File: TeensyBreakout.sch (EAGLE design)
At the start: 74 parts, among them IC1 MCP73871

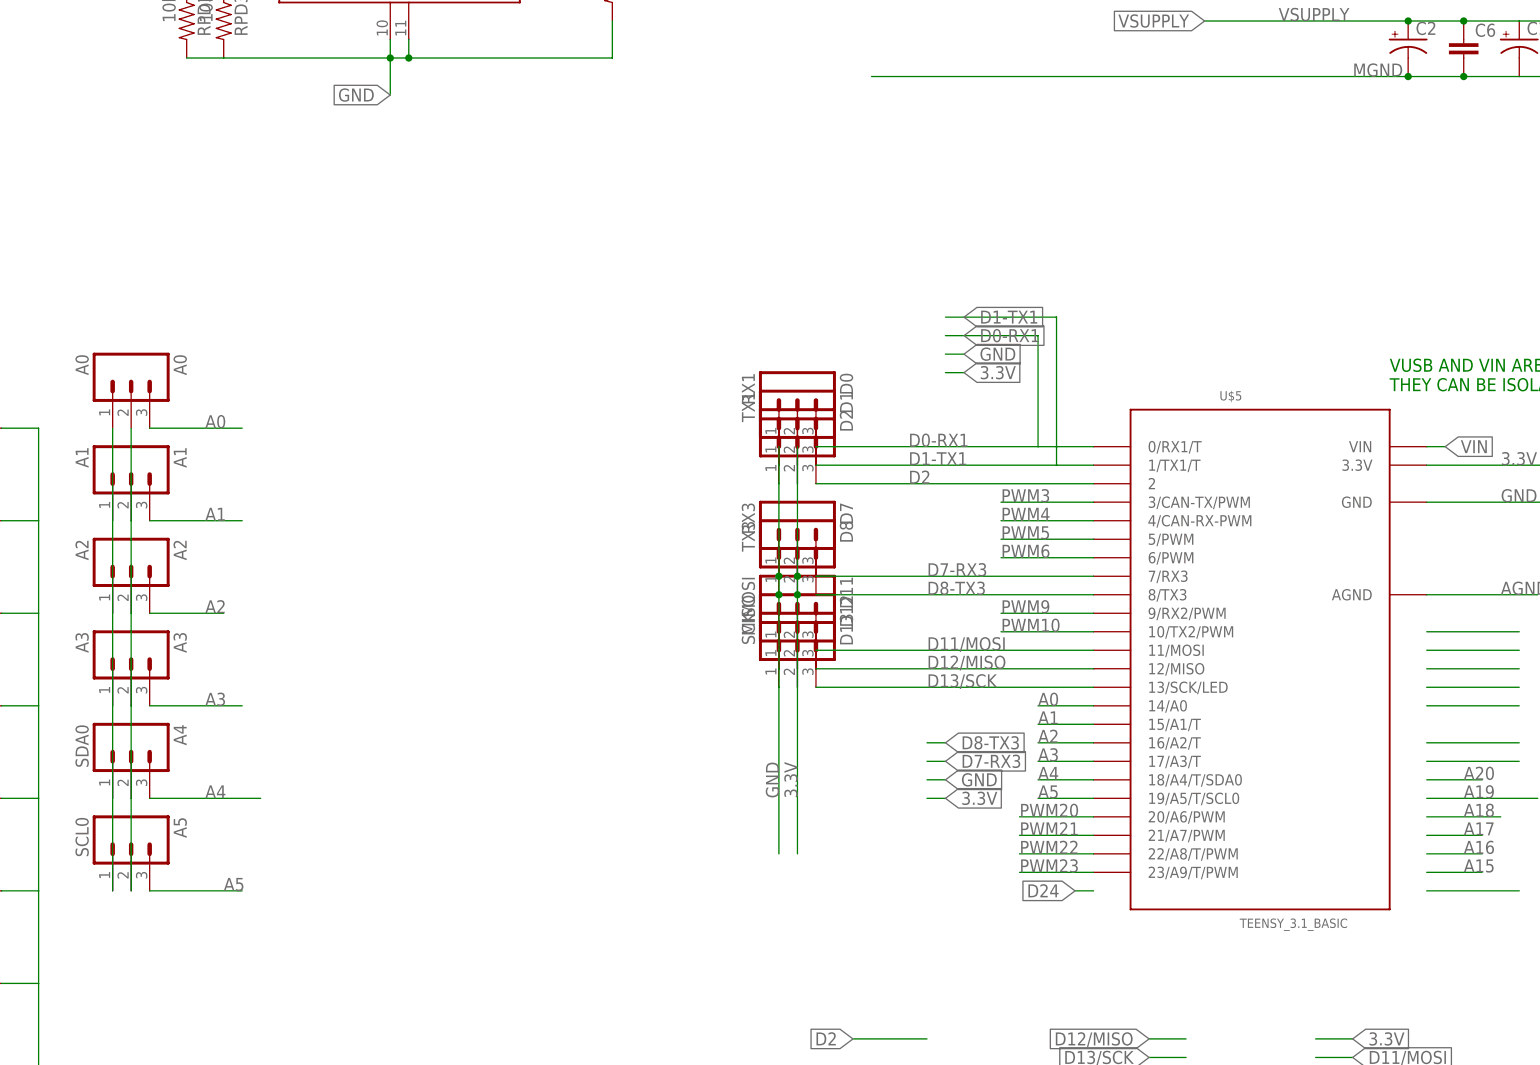
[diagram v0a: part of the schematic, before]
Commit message: Update locking headers, fix 2 missing wires
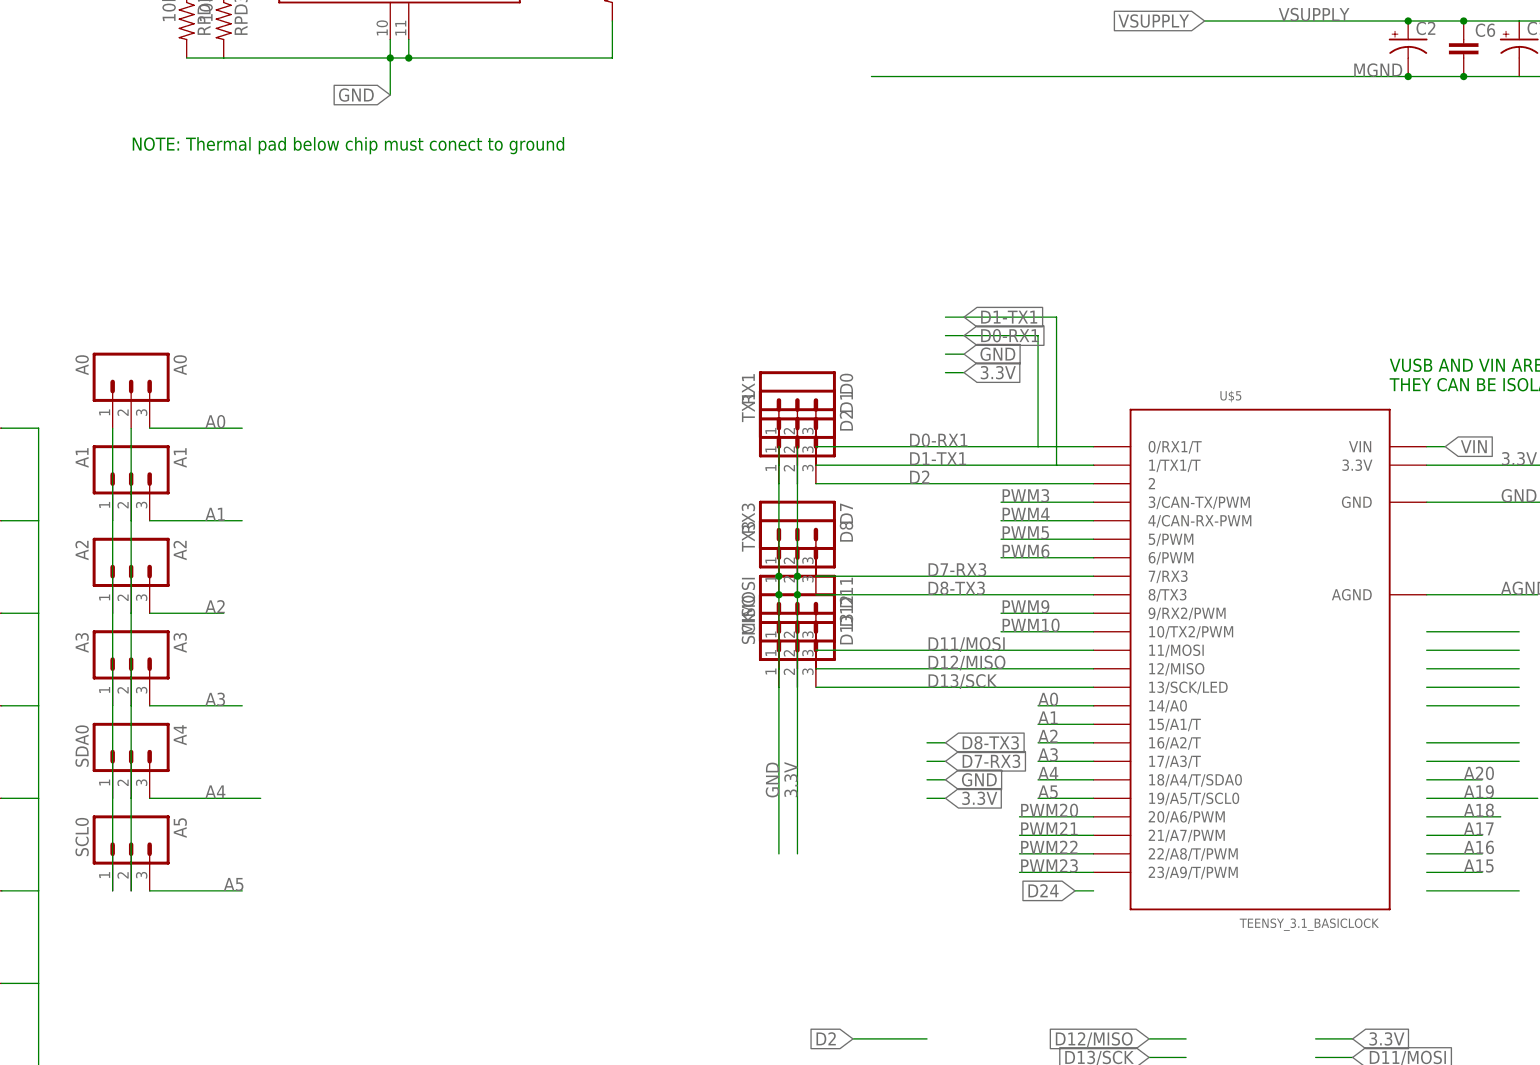
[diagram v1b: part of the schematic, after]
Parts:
- A0, A1, A2, A3, A4, A5, D0, D1, D10, D10M, D11, D12, D13, D2, D20M, D21M, D22M, D23M, D3, D3M, D4, D4M, D5, D5M, D6, D6M, D7, D8, D9, D9M: device SparkFun-Connectors:M03PTH -> tekdemo:M03LOCK
- U$5: value TEENSY_3.1_BASIC -> TEENSY_3.1_BASICLOCK; device tekdemo:TEENSY_3.1_BASIC -> tekdemo:TEENSY_3.1_BASICLOCK
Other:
- note added: "NOTE: Thermal pad below chip must conect to ground"
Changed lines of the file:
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@@
 </classes>
 <parts>
-<part name="D3M" library="SparkFun-Connectors" deviceset="M03" device="PTH" value="PWM"/>
-<part name="D4M" library="SparkFun-Connectors" deviceset="M03" device="PTH" value="PWM"/>
-<part name="D5M" library="SparkFun-Connectors" deviceset="M03" device="PTH" value="PWM"/>
-<part name="D6M" library="SparkFun-Connectors" deviceset="M03" device="PTH" value="PWM"/>
-<part name="D9M" library="SparkFun-Connectors" deviceset="M03" device="PTH" value="PWM"/>
-<part name="D10M" library="SparkFun-Connectors" deviceset="M03" device="PTH" value="PWM"/>
-<part name="D20M" library="SparkFun-Connectors" deviceset="M03" device="PTH" value="PWM"/>
-<part name="D21M" library="SparkFun-Connectors" deviceset="M03" device="PTH" value="PWM"/>
-<part name="D22M" library="SparkFun-Connectors" deviceset="M03" device="PTH" value="PWM"/>
-<part name="D23M" library="SparkFun-Connectors" deviceset="M03" device="PTH" value="PWM"/>
-<part name="A0" library="SparkFun-Connectors" deviceset="M03" device="PTH" value="A0"/>
-<part name="A1" library="SparkFun-Connectors" deviceset="M03" device="PTH" value="A1"/>
-<part name="A2" library="SparkFun-Connectors" deviceset="M03" device="PTH" value="A2"/>
-<part name="A3" library="SparkFun-Connectors" deviceset="M03" device="PTH" value="A3"/>
-<part name="A4" library="SparkFun-Connectors" deviceset="M03" device="PTH" value="SDA0"/>
-<part name="A5" library="SparkFun-Connectors" deviceset="M03" device="PTH" value="SCL0"/>
+<part name="D3M" library="tekdemo" deviceset="M03" device="LOCK" value="PWM"/>
+<part name="D4M" library="tekdemo" deviceset="M03" device="LOCK" value="PWM"/>
+<part name="D5M" library="tekdemo" deviceset="M03" device="LOCK" value="PWM"/>
+<part name="D6M" library="tekdemo" deviceset="M03" device="LOCK" value="PWM"/>
+<part name="D9M" library="tekdemo" deviceset="M03" device="LOCK" value="PWM"/>
+<part name="D10M" library="tekdemo" deviceset="M03" device="LOCK" value="PWM"/>
+<part name="D20M" library="tekdemo" deviceset="M03" device="LOCK" value="PWM"/>
+<part name="D21M" library="tekdemo" deviceset="M03" device="LOCK" value="PWM"/>
+<part name="D22M" library="tekdemo" deviceset="M03" device="LOCK" value="PWM"/>
+<part name="D23M" library="tekdemo" deviceset="M03" device="LOCK" value="PWM"/>
+<part name="A0" library="tekdemo" deviceset="M03" device="LOCK" value="A0"/>
+<part name="A1" library="tekdemo" deviceset="M03" device="LOCK" value="A1"/>
+<part name="A2" library="tekdemo" deviceset="M03" device="LOCK" value="A2"/>
+<part name="A3" library="tekdemo" deviceset="M03" device="LOCK" value="A3"/>
+<part name="A4" library="tekdemo" deviceset="M03" device="LOCK" value="SDA0"/>
+<part name="A5" library="tekdemo" deviceset="M03" device="LOCK" value="SCL0"/>
 <part name="R3" library="tekdemo" deviceset="RESISTOR" device="UNIVERSAL" value="200"/>
 <part name="LED3" library="tekdemo" deviceset="LED" device="UNIVERSAL"/>
@@
 <part name="R23" library="tekdemo" deviceset="RESISTOR" device="UNIVERSAL"/>
 <part name="LED23" library="tekdemo" deviceset="LED" device="UNIVERSAL"/>
-<part name="D11" library="SparkFun-Connectors" deviceset="M03" device="PTH" value="MOSI"/>
-<part name="D12" library="SparkFun-Connectors" deviceset="M03" device="PTH" value="MISO"/>
-<part name="D13" library="SparkFun-Connectors" deviceset="M03" device="PTH" value="SCK"/>
-<part name="D7" library="SparkFun-Connectors" deviceset="M03" device="PTH" value="RX3"/>
-<part name="D8" library="SparkFun-Connectors" deviceset="M03" device="PTH" value="TX3"/>
+<part name="D11" library="tekdemo" deviceset="M03" device="LOCK" value="MOSI"/>
+<part name="D12" library="tekdemo" deviceset="M03" device="LOCK" value="MISO"/>
+<part name="D13" library="tekdemo" deviceset="M03" device="LOCK" value="SCK"/>
+<part name="D7" library="tekdemo" deviceset="M03" device="LOCK" value="RX3"/>
+<part name="D8" library="tekdemo" deviceset="M03" device="LOCK" value="TX3"/>
 <part name="C2" library="tekdemo" deviceset="CAP-POLARIZED" device="UNIVERSAL"/>
 <part name="C10" library="tekdemo" deviceset="CAP-POLARIZED" device="UNIVERSAL"/>
 <part name="C7" library="tekdemo" deviceset="CAP-POLARIZED" device="UNIVERSAL"/>
 <part name="MCP1703" library="tekdemo" deviceset="VOLTAGE-REGULATOR" device="MCP1703" value="MCP1703"/>
-<part name="D2" library="SparkFun-Connectors" deviceset="M03" device="PTH"/>
-<part name="D1" library="SparkFun-Connectors" deviceset="M03" device="PTH" value="TX1"/>
-<part name="D0" library="SparkFun-Connectors" deviceset="M03" device="PTH" value="RX1"/>
-<part name="D3" library="SparkFun-Connectors" deviceset="M03" device="PTH" value="PWM"/>
-<part name="D4" library="SparkFun-Connectors" deviceset="M03" device="PTH" value="PWM"/>
-<part name="D5" library="SparkFun-Connectors" deviceset="M03" device="PTH" value="PWM"/>
-<part name="D6" library="SparkFun-Connectors" deviceset="M03" device="PTH" value="PWM"/>
-<part name="D9" library="SparkFun-Connectors" deviceset="M03" device="PTH" value="PWM"/>
-<part name="D10" library="SparkFun-Connectors" deviceset="M03" device="PTH" value="PWM"/>
+<part name="D2" library="tekdemo" deviceset="M03" device="LOCK"/>
+<part name="D1" library="tekdemo" deviceset="M03" device="LOCK" value="TX1"/>
+<part name="D0" library="tekdemo" deviceset="M03" device="LOCK" value="RX1"/>
+<part name="D3" library="tekdemo" deviceset="M03" device="LOCK" value="PWM"/>
+<part name="D4" library="tekdemo" deviceset="M03" device="LOCK" value="PWM"/>
+<part name="D5" library="tekdemo" deviceset="M03" device="LOCK" value="PWM"/>
+<part name="D6" library="tekdemo" deviceset="M03" device="LOCK" value="PWM"/>
+<part name="D9" library="tekdemo" deviceset="M03" device="LOCK" value="PWM"/>
+<part name="D10" library="tekdemo" deviceset="M03" device="LOCK" value="PWM"/>
 <part name="U$4" library="SMDuino" deviceset="ARDUINO" device=""/>
 <part name="IC1" library="adafruit" deviceset="MCP73871" device=""/>
-<part name="U$5" library="tekdemo" deviceset="TEENSY_3.1_BASIC" device=""/>
+<part name="U$5" library="tekdemo" deviceset="TEENSY_3.1_BASIC" device="LOCK"/>
 <part name="RTH" library="tekdemo" deviceset="RESISTOR" device="UNIVERSAL" value="10K"/>
 <part name="CSUP" library="tekdemo" deviceset="CAP-POLARIZED" device="UNIVERSAL" value="10UF"/>
@@
 THEY CAN BE ISOLATED ON BACKSIDE OF TEENSY BY CUTTING TRACES
 </text>
+<text x="-121.92" y="116.84" size="1.778" layer="91">NOTE: Thermal pad below chip must conect to ground</text>
 </plain>
 <instances>

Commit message: Improve documentation
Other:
- note added: "Breakout Wiring + LEDs"
- note added: "LIPO + power management"
- note added: "Voltage regulation"
- moved on the sheet: C1, C3, C4, C5, CBAT, CSUP, CSUP1, CSUP2, D0, D1, D11, D12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
